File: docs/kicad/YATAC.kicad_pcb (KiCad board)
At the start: 2 copper layers, 127 x 203.2 mm, 113 parts, among them J1 POWER IN, J2 POWER OUT, J3 AUDIO OUT, J4 KEYBOARD, J5 SERIAL, J6 DISPLAY, J7 EXPANSION, Q1 DS1233, Q2 2N3904, Q3 2N3904, Q4 BS170, SW1 RESET, U1 74F00, U10 74F574, U11 74F574, U12 74F574, U13 74F138, U14 PAL16R4, U15 27C020, U16 AS6C4008, U17 74F574, U18 74F574, U19 74F163, U2 74F08, U20 74F163, U21 74F541, U22 74F574, U23 74F574, U24 74F257, U25 74F574, U26 74F574, U27 74F574, U28 74F574, U29 74F244, U3 74F08, U30 74F541, U31 74F163, U32 74F163, U33 74F541, U34 74F574, U35 74F574, U36 74F541, U37 74F574, U38 74F299, U39 74F574, U4 74F32, U40 74F157, U41 74HCT4053, U42 MAX232, U43 NJM4580, U5 74F32, U6 74F32, U7 74ALS139, U8 74ALS139, U9 74F175, Y1 32M

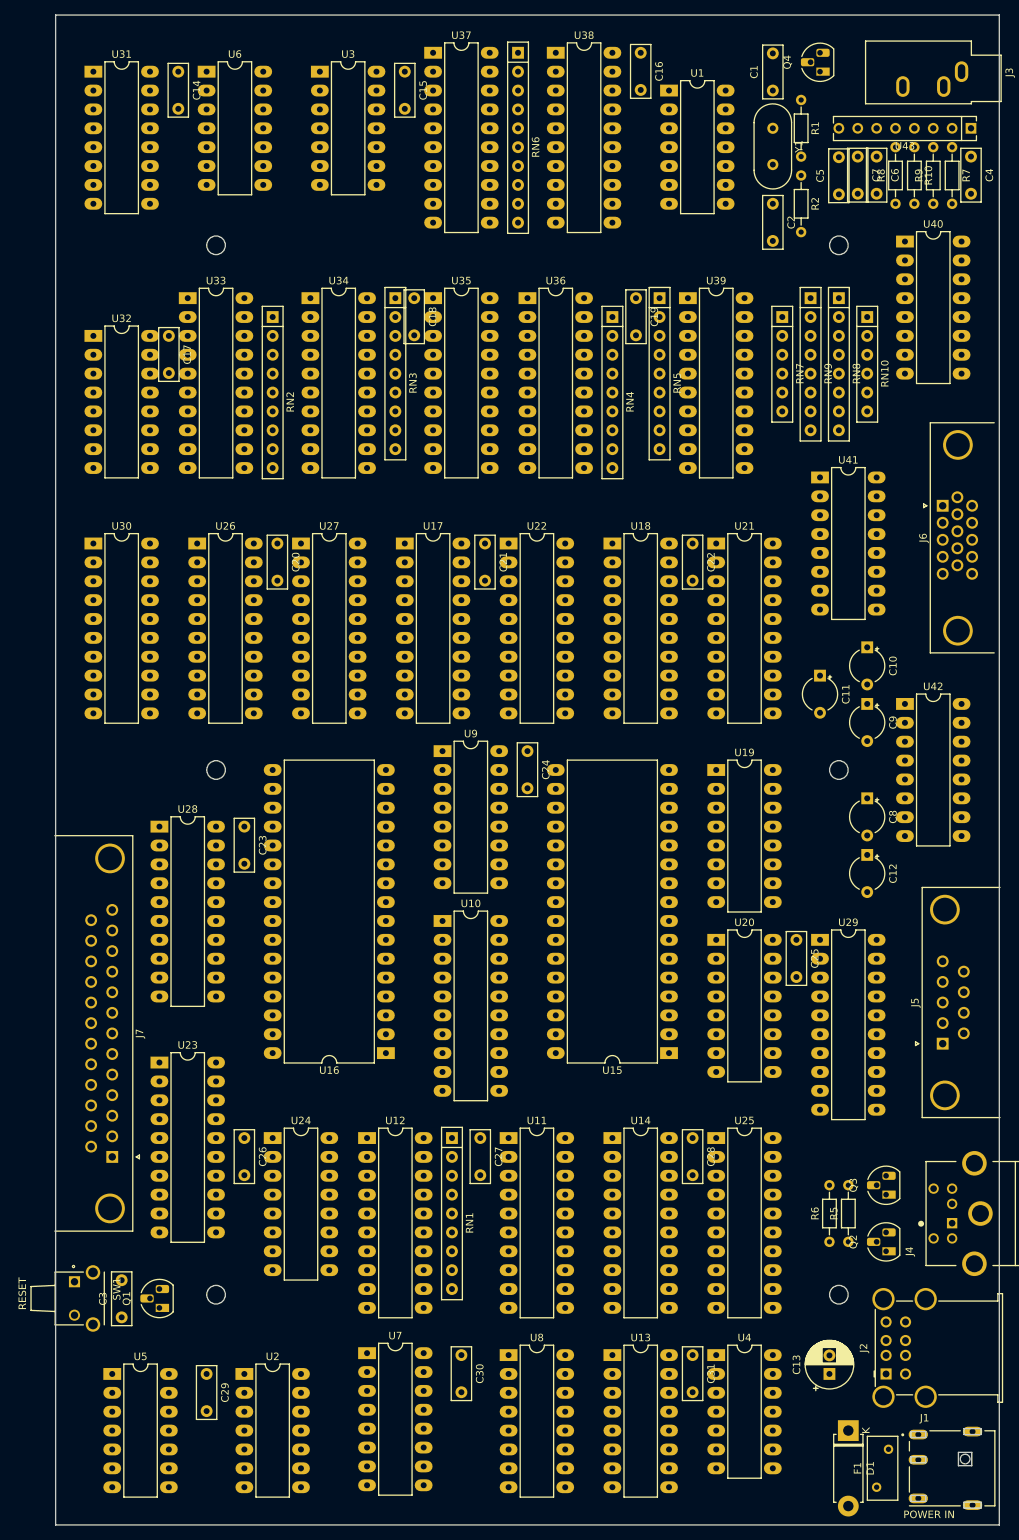
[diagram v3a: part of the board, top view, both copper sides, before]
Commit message: schematic with updated instruction encoding
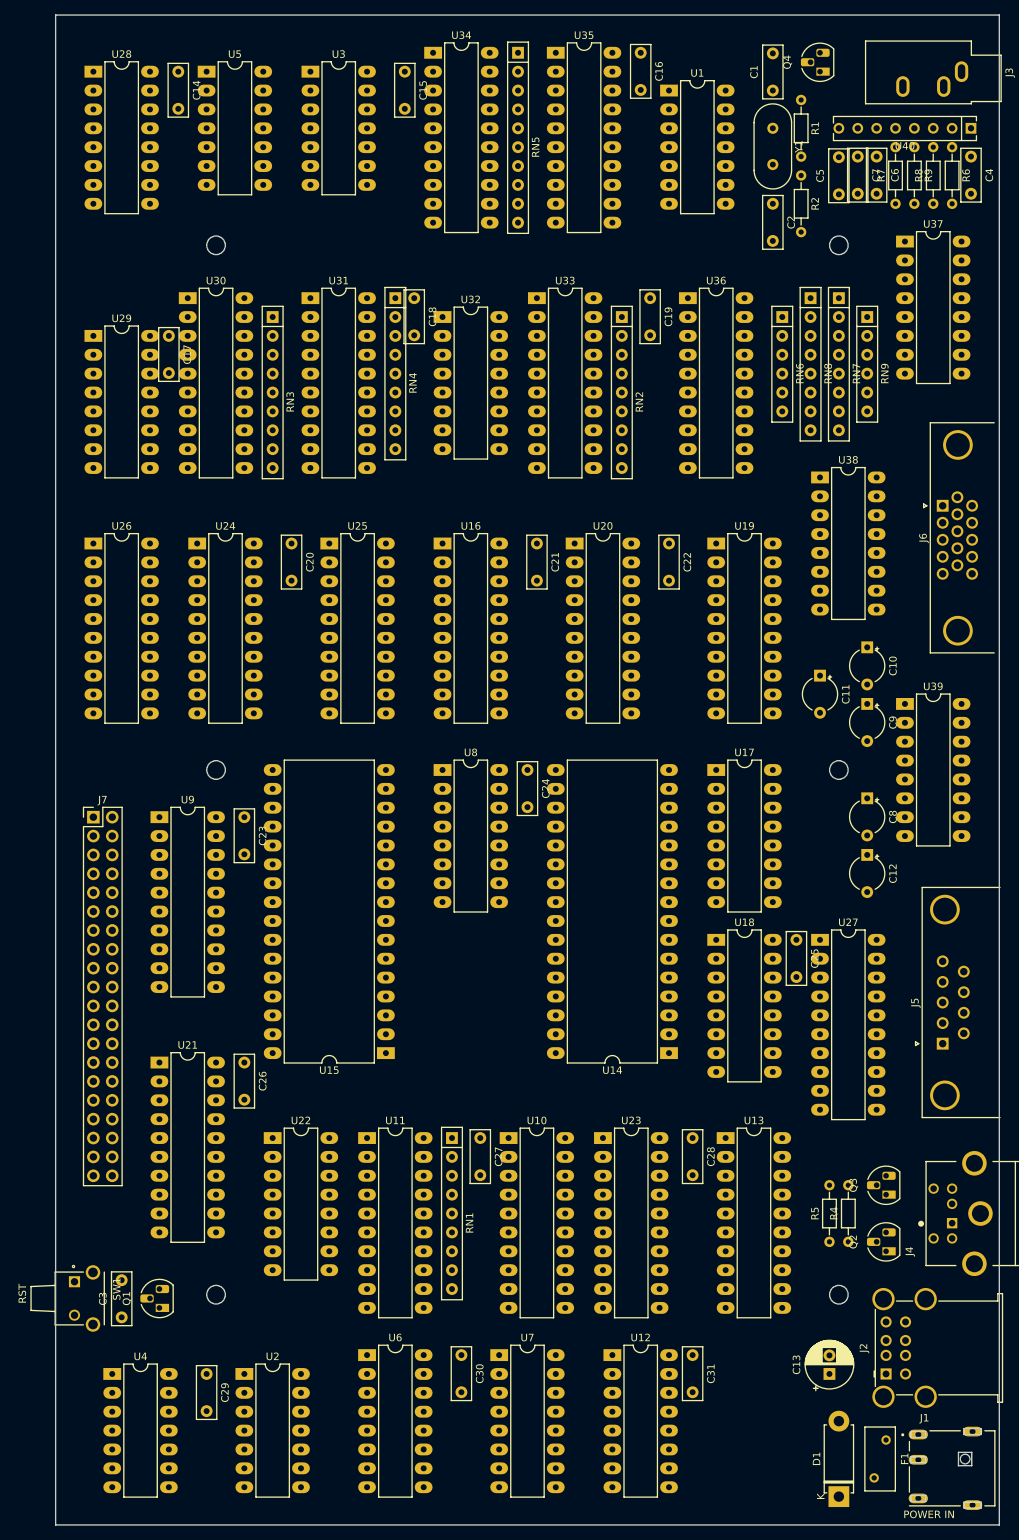
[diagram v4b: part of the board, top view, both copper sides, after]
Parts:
- removed the RN5 at (119.4, 76.2)
- removed the U11 at (99.1, 189.2)
- removed the U18 at (113.0, 109.2)
- removed the U25 at (127.0, 189.2)
- removed the U28 at (52.1, 147.3)
- removed the U30 at (43.2, 109.2)
- removed the U35 at (88.9, 76.2)
- removed the U8 at (99.1, 218.4)
- added U23: 74F574, Package_DIP:DIP-20_W7.62mm_LongPads, F.Cu at (111.8, 189.2)
- added U26: 74F574, Package_DIP:DIP-20_W7.62mm_LongPads, F.Cu at (43.2, 109.2)
- added U32: 74F174, Package_DIP:DIP-16_W7.62mm_LongPads, F.Cu at (90.2, 78.7)
- added U9: 74F574, Package_DIP:DIP-20_W7.62mm_LongPads, F.Cu at (52.1, 146.1)
- J7: footprint Connector_Dsub:DSUB-25_Female_Horizontal_P2.77x2.84mm_EdgePinOffset4.94mm_Housed_MountingHolesOffset7.48mm -> Connector_PinHeader_2.54mm:PinHeader_2x20_P2.54mm_Vertical
- RN6: renamed from RN7; value 470 -> 220
- RN7: renamed from RN8; value 3300 -> 1600
- RN8: renamed from RN9; value 3300 -> 1600
- RN9: renamed from RN10; value 1500 -> 680
- SW1: value RESET -> RST
- U1: value 74F00 -> 74F04
- U15: renamed from U16; value AS6C4008 -> AS6C1008
- U6: value 74F32 -> 74ALS139; footprint Package_DIP:DIP-14_W7.62mm_LongPads -> Package_DIP:DIP-16_W7.62mm_LongPads
- moved U5 175.7 mm to (58.4, 45.7)
- moved U6 174.1 mm to (80.0, 218.4)
- moved U4 81.3 mm to (45.7, 221.0)
- moved J7 45.8 mm to (43.2, 146.1), turned to 0 degrees
- moved U10 30.5 mm to (99.1, 189.2)
- moved U7 17.8 mm to (97.8, 218.4)
- moved U13 15.2 mm to (128.3, 189.2)
- moved C26 10.2 mm to (63.5, 179.1)
- moved D1 8.98 mm to (143.5, 237.5), turned to 90 degrees
- moved U20 8.89 mm to (108.0, 109.2)
- moved C21 6.98 mm to (102.9, 109.2)
- moved F1 6.48 mm to (149.9, 229.9), turned to 270 degrees
- moved U16 5.08 mm to (90.2, 109.2)
- moved U25 3.81 mm to (74.9, 109.2)
- moved C22 3.17 mm to (120.7, 109.2)
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- renumbered R5 to R4, R6 to R5, R7 to R6, R8 to R7, R9 to R8, R10 to R9, RN4 to RN2, RN2 to RN3, RN3 to RN4, RN6 to RN5, U12 to U11, U13 to U12, U14 to U13, U15 to U14, U17 to U16, U19 to U17, U20 to U18, U21 to U19, U22 to U20, U23 to U21, U24 to U22, U26 to U24, U27 to U25, U29 to U27, U31 to U28, U32 to U29, U33 to U30, U34 to U31, U36 to U33, U37 to U34, U38 to U35, U39 to U36, U40 to U37, U41 to U38, U42 to U39, U43 to U40, U9 to U8
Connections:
- J7 pad 1: ~rom2 -> pclk2
- J7 pad 10: DD7 -> DD5
- J7 pad 11: DD6 -> DD4
- J7 pad 12: DD5 -> DD3
- J7 pad 13: DD4 -> DD2
- J7 pad 14: 1 -> DD1
- J7 pad 15: 1 -> DD0
- J7 pad 16: qclk1 -> 0
- J7 pad 17: eclk -> I8
- J7 pad 18: ~eoe -> I1
- J7 pad 2: PD7 -> qclk2
- J7 pad 20: I1 -> 0
- J7 pad 21: I2 -> DD7
- J7 pad 22: I15 -> DD6
- J7 pad 23: 0 -> DD5
- J7 pad 24: 0 -> DD4
- J7 pad 25: 0 -> PD0
- J7 pad 3: PD6 -> ~rst
- J7 pad 4: PD5 -> Q
- J7 pad 5: PD4 -> I10
- J7 pad 6: PD3 -> I9
- J7 pad 7: PD2 -> 0
- J7 pad 8: PD1 -> DD7
- J7 pad 9: PD0 -> DD6
- U1 pad 10: cclk -> /GPU/~cle
- U1 pad 11: hblank -> Net-(U1-Pad11)
- U1 pad 12: Net-(U1-Pad12) -> hblank
- U1 pad 13: Net-(U1-Pad12) -> Net-(U1-Pad13)
- U1 pad 2: Net-(C1-Pad1) -> cclk
- U1 pad 4: cclk -> dclk
- U1 pad 5: cclk -> I10
- U1 pad 6: dclk -> Net-(U1-Pad6)
- U1 pad 8: /GPU/~cle -> Net-(U1-Pad8)
- U10 pad 11: dclk -> ~ille
- U10 pad 12: ~hloe -> I7
- U10 pad 13: ~alue -> I6
- U10 pad 14: ~pcoe -> I5
- U10 pad 15: ~pgoe -> I4
- U10 pad 16: ~yoe -> I3
- U10 pad 17: ~voe -> I2
- U10 pad 18: ~hsync -> I1
- U10 pad 19: Net-(U10-Pad19) -> I0
- U10 pad 2: ~inst -> PD0
- U10 pad 3: ~gsync -> PD1
- U10 pad 4: Net-(U10-Pad4) -> PD2
- U10 pad 5: Net-(U10-Pad5) -> PD3
- U10 pad 6: Net-(U10-Pad6) -> PD4
- U10 pad 7: Net-(U10-Pad7) -> PD5
- U10 pad 8: Net-(U10-Pad8) -> PD6
- U10 pad 9: Net-(U10-Pad9) -> PD7
- U12 pad 10: ~ele -> ~hlle
- U12 pad 11: ~hlle -> ~yle
- U12 pad 14: ~pcle -> ~ele
- U12 pad 15: ~pgle -> ~xle
- U12 pad 3: I2 -> I8
- U12 pad 5: ~rom2 -> ~romw
- U12 pad 6: I15 -> I9
- U12 pad 7: ~yle -> ~pgle
- U12 pad 9: ~xle -> ~pcle
- U13 pad 12: DD7 -> ~prog
- U13 pad 13: mv -> pcent
- U13 pad 14: ~inst -> Net-(U13-Pad14)
- U13 pad 15: hsel -> boot
- U13 pad 16: boot -> hsel
- U13 pad 17: Net-(U14-Pad17) -> ~fetch
- U13 pad 18: pcent -> PA16
- U13 pad 19: PA16 -> PA17
- U13 pad 5: I3 -> DD7
- U14 pad 30: ~pcoe -> PA17
- U15 pad 1: DA18 -> 1
- U15 pad 30: DA17 -> 1
- U16 pad 1: pclk1 -> pcoe
- U16 pad 11: qclk1 -> mclk
- U19 pad 1: ~pcoe -> ~prog
- U19 pad 19: ~pcoe -> qclk1
- U2 pad 10: I6 -> Net-(U2-Pad10)
- U2 pad 11: ~aoe -> ~doe
- U2 pad 12: ~ram2 -> Net-(U2-Pad12)
- U2 pad 13: Net-(U2-Pad13) -> qclk1
- U2 pad 4: ~pgle -> ~rst
- U2 pad 5: ~rst -> ~pgle
- U2 pad 8: Net-(U2-Pad8) -> ~aoe
- U2 pad 9: ~inst -> ~ramw
- U22 pad 15: ~hloe -> ~alue
- U24 pad 1: pclk1 -> ~xoe
- U25 pad 1: ~yoe -> pclk1
- U27 pad 11: I8 -> I12
- U27 pad 13: I9 -> I13
- U27 pad 15: I10 -> I14
- U27 pad 17: I11 -> I15
- U28 pad 13: eclk -> /GPU/H1
- U3 pad 10: mode1 -> Net-(U3-Pad10)
- U3 pad 11: ~doe -> DA16
- U3 pad 12: Net-(U3-Pad12) -> qclk1
- U3 pad 13: qclk1 -> Net-(U1-Pad6)
- U3 pad 4: Net-(U3-Pad3) -> nclk
- U3 pad 5: nclk -> Net-(U3-Pad3)
- U3 pad 6: Net-(U1-Pad9) -> Net-(U3-Pad10)
- U3 pad 8: Net-(U3-Pad8) -> Net-(U1-Pad11)
- U3 pad 9: mode0 -> cclk
- U30 pad 3: eclk -> /GPU/H1
- U35 pad 19: Net-(U1-Pad9) -> Net-(U3-Pad10)
- U38 pad 10: Net-(U3-Pad8) -> vdacsel
- U38 pad 11: Net-(U3-Pad8) -> vdacsel
- U38 pad 9: Net-(U3-Pad8) -> vdacsel
- U4 pad 1: Eo4 -> hblank
- U4 pad 10: Net-(U4-Pad10) -> Net-(U1-Pad9)
- U4 pad 11: Net-(U4-Pad10) -> ~ale
- U4 pad 12: pclk1 -> ~alue
- U4 pad 13: I14 -> I5
- U4 pad 2: Net-(U4-Pad10) -> rclk
- U4 pad 3: DA16 -> Net-(U4-Pad3)
- U4 pad 4: Eo5 -> qclk1
- U4 pad 5: Net-(U4-Pad10) -> I3
- U4 pad 6: DA17 -> Net-(U4-Pad6)
- U4 pad 8: DA18 -> Net-(U4-Pad8)
- U4 pad 9: Eo6 -> boot
- U5 pad 1: hblank -> I2
- U5 pad 10: Net-(U10-Pad7) -> Net-(U1-Pad13)
- U5 pad 11: Net-(U10-Pad9) -> Net-(U1-Pad13)
- U5 pad 12: Net-(U10-Pad8) -> /GPU/H6
- U5 pad 13: mv -> /GPU/H7
- U5 pad 2: rclk -> ~ramw
- U5 pad 3: Net-(U10-Pad4) -> ~dwe
- U5 pad 4: sclk -> mode1
- U5 pad 5: I13 -> /GPU/H0
- U5 pad 6: Net-(U10-Pad5) -> Net-(U3-Pad2)
- U5 pad 8: Net-(U10-Pad6) -> ~gsync
- U5 pad 9: boot -> /GPU/H4
- U6 pad 1: I12 -> 0
- U6 pad 10: Net-(U1-Pad12) -> Net-(U2-Pad10)
- U6 pad 11: Net-(U1-Pad12) -> ~eoe
- U6 pad 12: /GPU/H6 -> ~inoe
- U6 pad 13: /GPU/H7 -> I11
- U6 pad 14: 1 -> I4
- U6 pad 2: ~ram2 -> qclk1
- U6 pad 3: ~dwe -> ~read
- U6 pad 4: mode1 -> Net-(U6-Pad4)
- U6 pad 5: /GPU/H0 -> ~ramr
- U6 pad 6: Net-(U3-Pad2) -> ~romw
- U6 pad 7: 0 -> ~ramw
- U6 pad 8: ~gsync -> 0
- U6 pad 9: /GPU/H4 -> Net-(U2-Pad12)
- U7 pad 1: rclk -> qclk1
- U7 pad 10: ~eoe -> Net-(U1-Pad9)
- U7 pad 11: ~xroe -> Net-(U7-Pad11)
- U7 pad 12: Net-(U2-Pad13) -> Net-(U7-Pad12)
- U7 pad 13: I4 -> ~rst
- U7 pad 14: I3 -> ~prog
- U7 pad 15: ~ram1 -> rclk
- U7 pad 2: Net-(U2-Pad8) -> hsel
- U7 pad 3: ~rst -> ~fetch
- U7 pad 4: Net-(U7-Pad4) -> ~ille
- U7 pad 5: Net-(U7-Pad5) -> ~ihle
- U7 pad 6: Net-(U10-Pad7) -> Net-(U7-Pad6)
- U7 pad 7: Net-(U10-Pad8) -> Net-(U7-Pad7)
- U7 pad 9: Net-(U3-Pad12) -> Net-(U7-Pad9)

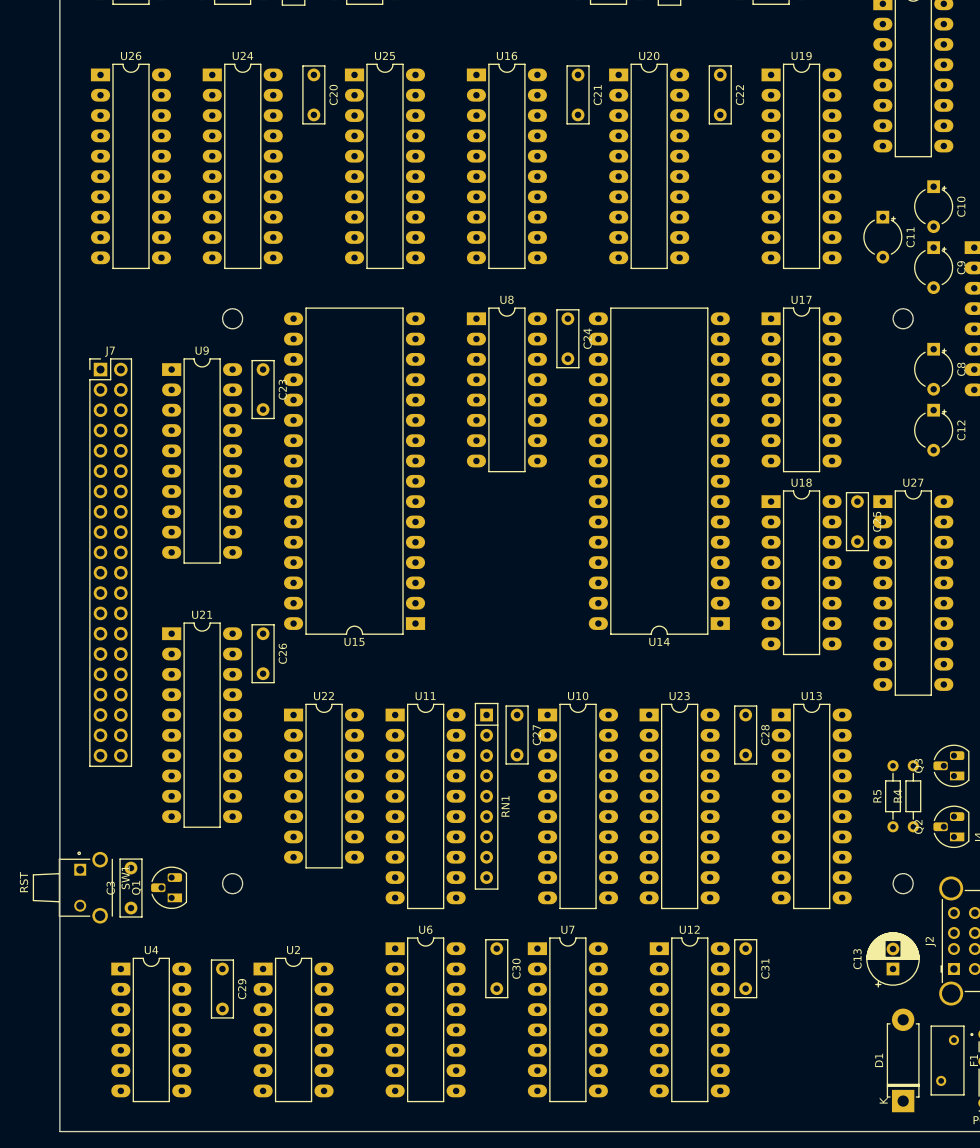
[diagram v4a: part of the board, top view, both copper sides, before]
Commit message: add LED, bump to 1.0.7
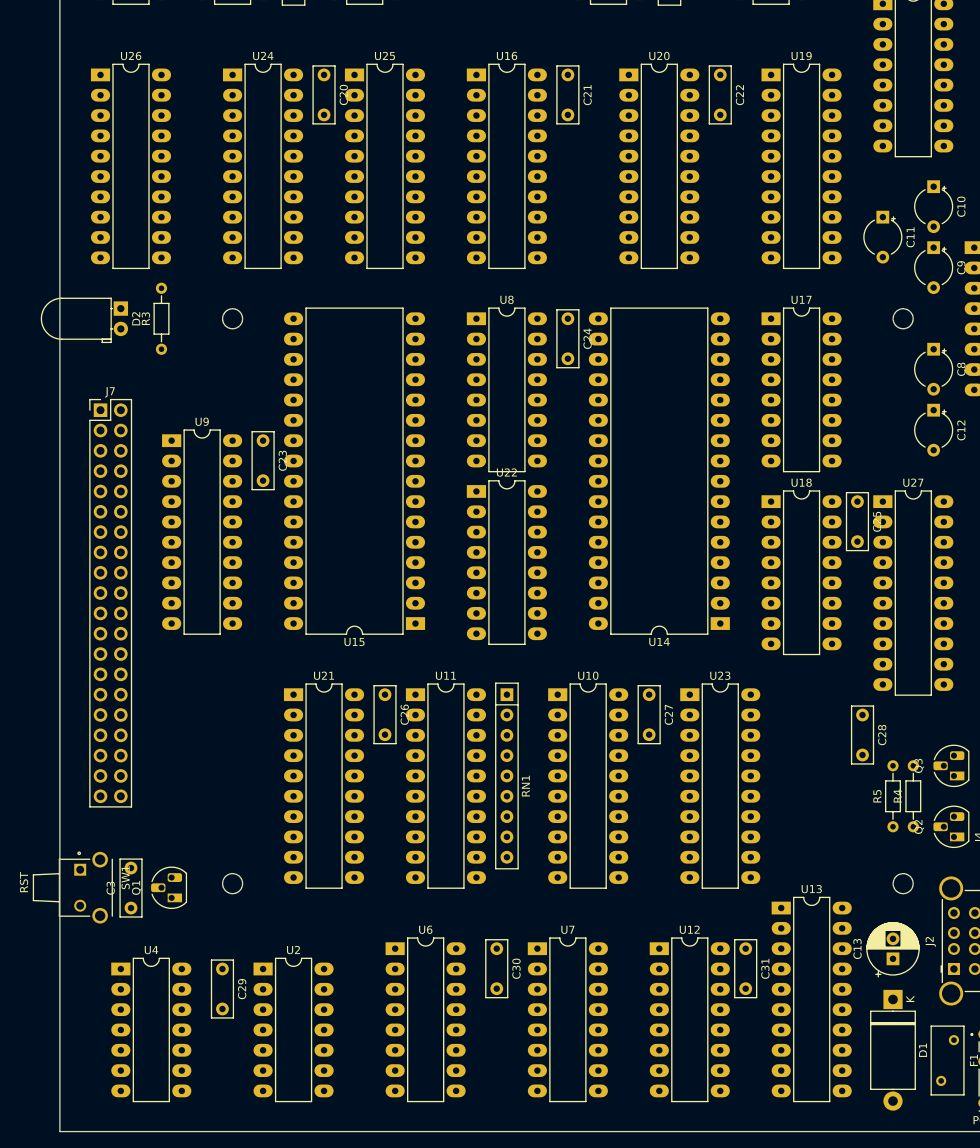
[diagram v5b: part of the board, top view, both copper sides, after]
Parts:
- added D2: Q LED, LED_THT:LED_D5.0mm_Horizontal_O1.27mm_Z3.0mm, F.Cu at (45.7, 138.4)
- added R3: 1.6k, Resistor_THT:R_Axial_DIN0204_L3.6mm_D1.6mm_P7.62mm_Horizontal, F.Cu at (50.8, 143.5)
- D1: footprint Diode_THT:D_5W_P10.16mm_Horizontal -> Diode_THT:D_DO-27_P12.70mm_Horizontal
- moved U22 36.1 mm to (90.2, 161.3)
- moved U13 24.1 mm to (128.3, 213.4)
- moved U21 17.0 mm to (67.3, 186.7)
- moved C26 17.0 mm to (78.7, 186.7)
- moved C27 16.7 mm to (111.8, 186.7)
- moved C28 14.6 mm to (138.4, 189.2)
- moved D1 12.8 mm to (142.2, 224.8), turned to 270 degrees
- moved C23 8.89 mm to (63.5, 154.9)
- moved U9 8.89 mm to (52.1, 154.9)
- moved U23 5.68 mm to (116.8, 186.7)
- moved J7 5.08 mm to (43.2, 151.1)
- moved RN1 3.59 mm to (94.0, 186.7)
- moved U11 3.59 mm to (82.5, 186.7)
- moved U10 2.84 mm to (100.3, 186.7)
- moved U24 2.54 mm to (59.7, 109.2)
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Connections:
- net ~scle renamed ~sle
